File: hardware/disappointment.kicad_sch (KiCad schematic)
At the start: 52 parts, among them J1 Bus_ISA_16bit, J3 Conn_02x10_Odd_Even, J4 Conn_01x02, J5 ATX-24, U1 F85226AF

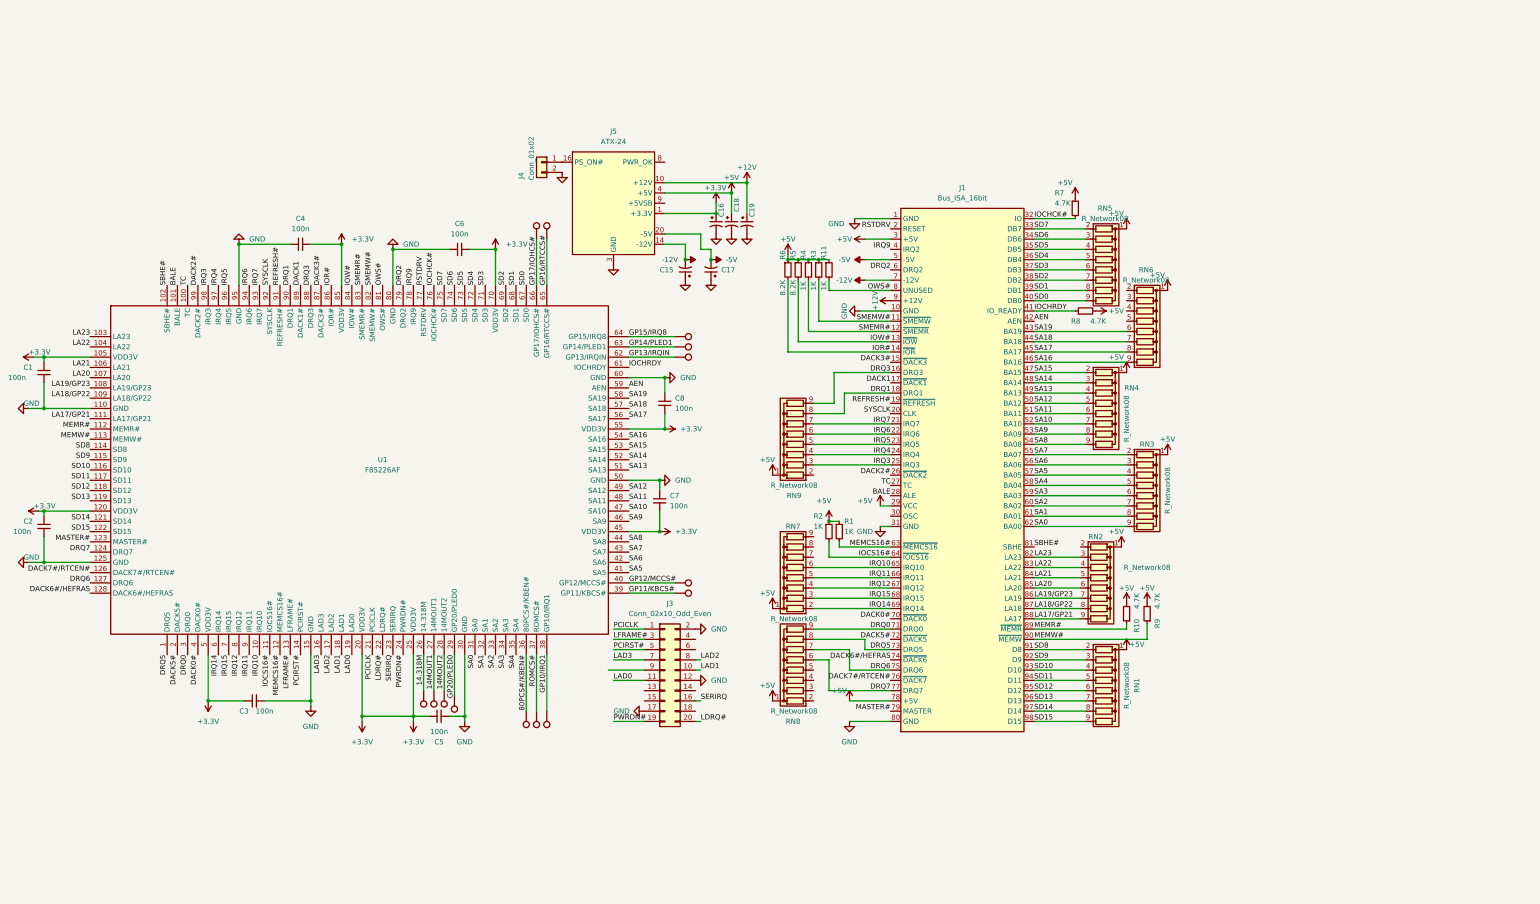
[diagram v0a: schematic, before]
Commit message: started rerouting PCB
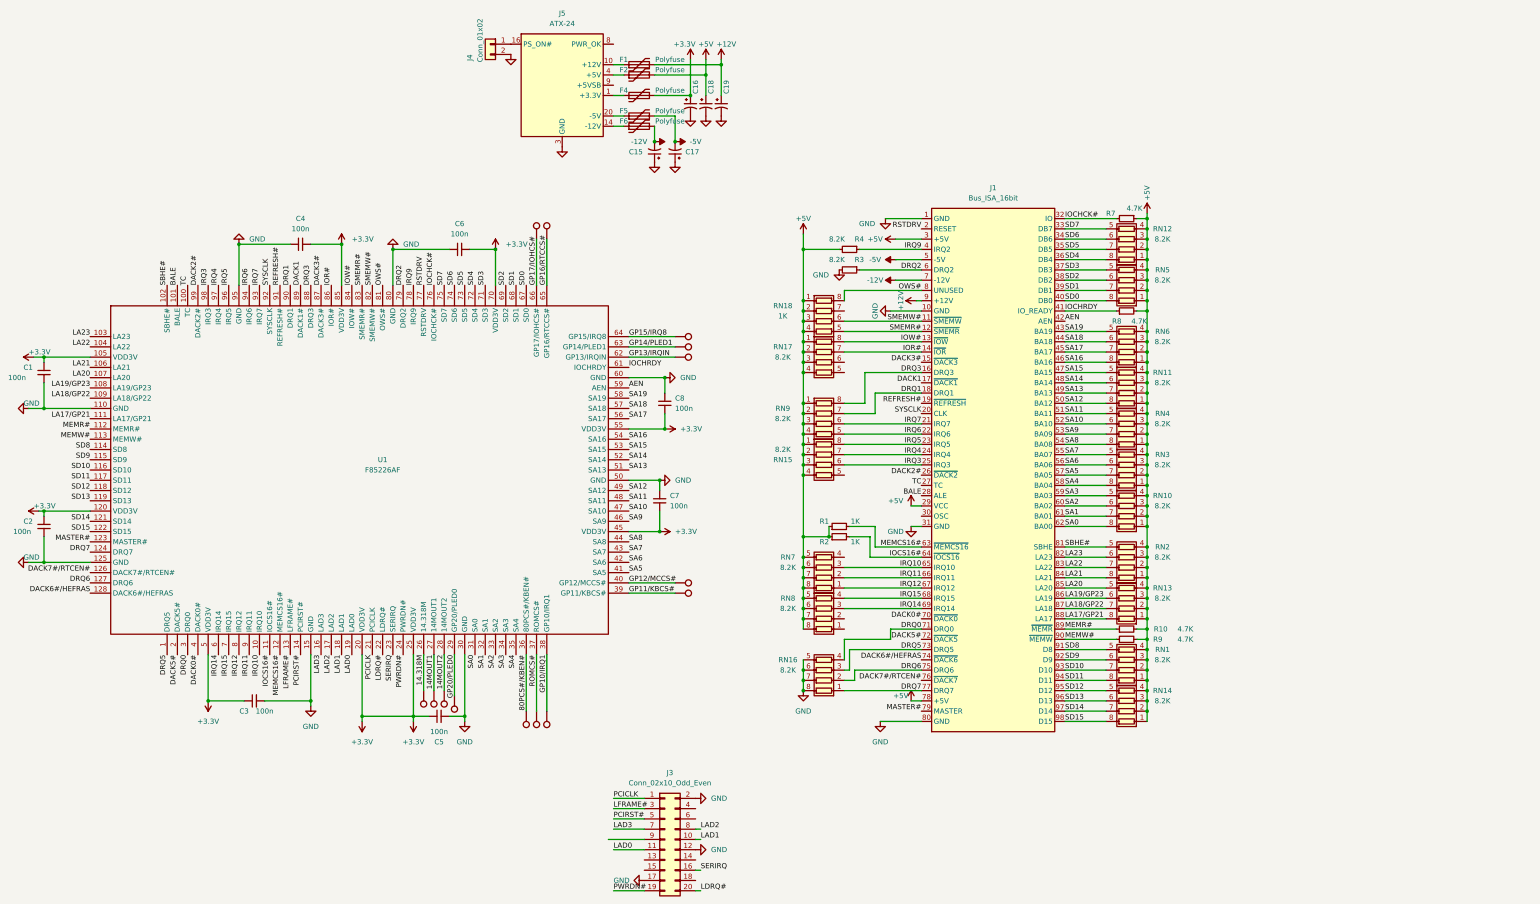
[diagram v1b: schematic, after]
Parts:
- removed R11: 1K, Resistor_SMD:R_1206_3216Metric_Pad1.30x1.75mm_HandSolder, symbol Device:R_Small
- removed R5, R6: 8.2K, Resistor_SMD:R_1206_3216Metric_Pad1.30x1.75mm_HandSolder, symbol Device:R_Small
- removed RN1, RN2, RN3, RN4, RN5, RN6, RN7, RN8, RN9: R_Network08, ps2usb:745C101, symbol Device:R_Network08
- added F1, F2, F4, F5, F6: Polyfuse, symbol Device:Polyfuse
- added RN1, RN10, RN11, RN12, RN13, RN14, RN15, RN16, RN17, RN2, RN3, RN4, RN5, RN6, RN7, RN8, RN9: 8.2K, Resistor_SMD:R_Array_Concave_4x0603, symbol Device:R_Pack04
- added RN18: 1K, Resistor_SMD:R_Array_Concave_4x0603, symbol Device:R_Pack04
- R3, R4: value 1K -> 8.2K
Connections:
- net +12V: now also F1.2; no longer J5.10 (+12V), J5.11 (+12V)
- net +3.3V: now also F4.2; no longer J5.1 (+3.3V), J5.12 (+3.3V), J5.13 (+3.3V), J5.2 (+3.3V)
- net +5V: now also R4.2, F2.2, RN1.1 (R1.1), RN1.2 (R2.1), RN1.3 (R3.1), RN1.4 (R4.1), RN10.1 (R1.1), RN10.2 (R2.1), RN10.3 (R3.1), RN10.4 (R4.1), RN11.1 (R1.1), RN11.2 (R2.1), RN11.3 (R3.1), RN11.4 (R4.1), RN12.1 (R1.1), RN12.2 (R2.1), RN12.3 (R3.1), RN12.4 (R4.1), RN13.1 (R1.1), RN13.2 (R2.1), RN13.3 (R3.1), RN13.4 (R4.1), RN14.1 (R1.1), RN14.2 (R2.1), RN14.3 (R3.1), RN14.4 (R4.1), RN15.1 (R1.1), RN15.2 (R2.1), RN15.3 (R3.1), RN15.4 (R4.1), RN17.1 (R1.1), RN17.2 (R2.1), RN17.3 (R3.1), RN17.4 (R4.1), RN18.1 (R1.1), RN18.2 (R2.1), RN18.3 (R3.1), RN18.4 (R4.1), RN2.1 (R1.1), RN2.2 (R2.1), RN2.3 (R3.1), RN2.4 (R4.1), RN3.1 (R1.1), RN3.2 (R2.1), RN3.3 (R3.1), RN3.4 (R4.1), RN4.1 (R1.1), RN4.2 (R2.1), RN4.3 (R3.1), RN4.4 (R4.1), RN5.1 (R1.1), RN5.2 (R2.1), RN5.3 (R3.1), RN5.4 (R4.1), RN6.1 (R1.1), RN6.2 (R2.1), RN6.3 (R3.1), RN6.4 (R4.1), RN7.5 (R4.2), RN7.6 (R3.2), RN7.7 (R2.2), RN7.8 (R1.2), RN8.5 (R4.2), RN8.6 (R3.2), RN8.7 (R2.2), RN8.8 (R1.2), RN9.1 (R1.1), RN9.2 (R2.1), RN9.3 (R3.1), RN9.4 (R4.1); no longer J5.21 (+5V), J5.22 (+5V), J5.23 (+5V), J5.4 (+5V), J5.6 (+5V), R3.1, R4.1
- net -12V: now also F6.2; no longer J5.14 (-12V)
- net -5V: now also F5.2; no longer J5.20 (NC)
- net DRQ0: now also RN16.4 (R4.1)
- net DRQ1: now also RN9.7 (R2.2)
- net DRQ2: now also R3.1
- net DRQ3: now also RN9.8 (R1.2)
- net DRQ5: now also RN16.3 (R3.1)
- net DRQ6: now also RN16.2 (R2.1)
- net DRQ7: now also RN16.1 (R1.1)
- net GND: now also R3.2, RN16.5 (R4.2), RN16.6 (R3.2), RN16.7 (R2.2), RN16.8 (R1.2)
- net IOR#: now also RN17.7 (R2.2)
- net IOW#: now also RN17.8 (R1.2)
- net IRQ10: now also RN7.3 (R3.1)
- net IRQ11: now also RN7.2 (R2.1)
- net IRQ12: now also RN7.1 (R1.1)
- net IRQ14: now also RN8.3 (R3.1)
- net IRQ15: now also RN8.4 (R4.1)
- net IRQ3: now also RN15.6 (R3.2)
- net IRQ4: now also RN15.7 (R2.2)
- net IRQ5: now also RN15.8 (R1.2)
- net IRQ6: now also RN9.5 (R4.2)
- net IRQ7: now also RN9.6 (R3.2)
- net IRQ9: now also R4.1
- net LA17/GP21: now also RN13.8 (R1.2)
- net LA18/GP22: now also RN13.7 (R2.2)
- net LA19/GP23: now also RN13.6 (R3.2)
- net LA20: now also RN13.5 (R4.2)
- net LA21: now also RN2.8 (R1.2)
- net LA22: now also RN2.7 (R2.2)
- net LA23: now also RN2.6 (R3.2)
- net OWS#: now also RN18.8 (R1.2)
- net SA0: now also RN10.8 (R1.2)
- net SA1: now also RN10.7 (R2.2)
- net SA10: now also RN4.6 (R3.2)
- net SA11: now also RN4.5 (R4.2)
- net SA12: now also RN11.8 (R1.2)
- net SA13: now also RN11.7 (R2.2)
- net SA14: now also RN11.6 (R3.2)
- net SA15: now also RN11.5 (R4.2)
- net SA16: now also RN6.8 (R1.2)
- net SA17: now also RN6.7 (R2.2)
- net SA18: now also RN6.6 (R3.2)
- net SA19: now also RN6.5 (R4.2)
- net SA2: now also RN10.6 (R3.2)
- net SA3: now also RN10.5 (R4.2)
- net SA4: now also RN3.8 (R1.2)
- net SA5: now also RN3.7 (R2.2)
- net SA6: now also RN3.6 (R3.2)
- net SA7: now also RN3.5 (R4.2)
- net SA8: now also RN4.8 (R1.2)
- net SA9: now also RN4.7 (R2.2)
- net SBHE#: now also RN2.5 (R4.2)
- net SD0: now also RN5.8 (R1.2)
- net SD1: now also RN5.7 (R2.2)
- net SD10: now also RN1.7 (R2.2)
- net SD11: now also RN1.8 (R1.2)
- net SD12: now also RN14.5 (R4.2)
- net SD13: now also RN14.6 (R3.2)
- net SD14: now also RN14.7 (R2.2)
- net SD15: now also RN14.8 (R1.2)
- net SD2: now also RN5.6 (R3.2)
- net SD3: now also RN5.5 (R4.2)
- net SD4: now also RN12.8 (R1.2)
- net SD5: now also RN12.7 (R2.2)
- net SD6: now also RN12.6 (R3.2)
- net SD7: now also RN12.5 (R4.2)
- net SD8: now also RN1.5 (R4.2)
- net SD9: now also RN1.6 (R3.2)
- net SMEMR#: now also RN18.5 (R4.2); no longer R4.2
- net SMEMW#: now also RN18.6 (R3.2); no longer R3.2
- net at J5.20 (NC): now also F5.1
- new net: F6.1, J5.14 (-12V)
- new net: F2.1, J5.21 (+5V), J5.22 (+5V), J5.23 (+5V), J5.4 (+5V), J5.6 (+5V)
- new net: F4.1, J5.1 (+3.3V), J5.12 (+3.3V), J5.13 (+3.3V), J5.2 (+3.3V)
- new net: F1.1, J5.10 (+12V), J5.11 (+12V)
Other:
- moved on the sheet: C15, C16, C17, C18, C19, J1, J3, J4, J5, R1, R10, R2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

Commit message: getting there
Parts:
- F1, F2, F4, F5, F6: footprint (none) -> Fuse:Fuse_1206_3216Metric
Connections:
- net DRQ0: now also RN16.1 (R1.1); no longer RN16.4 (R4.1)
- net DRQ5: now also RN16.2 (R2.1); no longer RN16.3 (R3.1)
- net DRQ6: now also RN16.3 (R3.1); no longer RN16.2 (R2.1)
- net DRQ7: now also RN16.4 (R4.1); no longer RN16.1 (R1.1)
- net IRQ10: now also RN7.2 (R2.1); no longer RN7.3 (R3.1)
- net IRQ11: now also RN7.3 (R3.1); no longer RN7.2 (R2.1)
- net IRQ12: now also RN7.4 (R4.1); no longer RN7.1 (R1.1)
- net IRQ14: now also RN8.2 (R2.1); no longer RN8.3 (R3.1)
- net IRQ15: now also RN8.1 (R1.1); no longer RN8.4 (R4.1)
- net at J5.20 (NC): now also F5.1

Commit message: getting there more
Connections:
- net OWS#: now also RN18.5 (R4.2); no longer RN18.8 (R1.2)
- net SMEMR#: now also RN18.8 (R1.2); no longer RN18.5 (R4.2)
- net SMEMW#: now also RN18.7 (R2.2); no longer RN18.6 (R3.2)
- net at J5.20 (NC): now also F5.1
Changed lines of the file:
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@@
   (junction (at 397.51 251.46) (diameter 0) (color 0 0 0 0)
   )
-  (junction (at 312.42 160.02) (diameter 0) (color 0 0 0 0)
-  )
   (junction (at 397.51 185.42) (diameter 0) (color 0 0 0 0)
   )
@@
   (junction (at 318.77 218.44) (diameter 0) (color 0 0 0 0)
   )
-  (junction (at 312.42 165.1) (diameter 0) (color 0 0 0 0)
-  )
   (junction (at 278.13 191.77) (diameter 0) (color 0 0 0 0)
   )
@@
   (junction (at 215.9 262.89) (diameter 0) (color 0 0 0 0)
   )
-  (junction (at 312.42 167.64) (diameter 0) (color 0 0 0 0)
-  )
   (junction (at 397.51 220.98) (diameter 0) (color 0 0 0 0)
   )
   (junction (at 280.67 120.65) (diameter 0) (color 0 0 0 0)
   )
+  (junction (at 312.42 165.1) (diameter 0) (color 0 0 0 0)
+  )
   (junction (at 397.51 193.04) (diameter 0) (color 0 0 0 0)
   )
@@
   (junction (at 397.51 175.26) (diameter 0) (color 0 0 0 0)
   )
-  (junction (at 312.42 162.56) (diameter 0) (color 0 0 0 0)
-  )
   (junction (at 397.51 203.2) (diameter 0) (color 0 0 0 0)
   )
@@
   (junction (at 198.12 146.05) (diameter 0) (color 0 0 0 0)
   )
+  (junction (at 312.42 167.64) (diameter 0) (color 0 0 0 0)
+  )
   (junction (at 312.42 172.72) (diameter 0) (color 0 0 0 0)
   )
@@
   (junction (at 284.48 109.22) (diameter 0) (color 0 0 0 0)
   )
+  (junction (at 312.42 162.56) (diameter 0) (color 0 0 0 0)
+  )
   (junction (at 312.42 236.22) (diameter 0) (color 0 0 0 0)
   )
@@
   (junction (at 312.42 195.58) (diameter 0) (color 0 0 0 0)
   )
+  (junction (at 312.42 160.02) (diameter 0) (color 0 0 0 0)
+  )
   (junction (at 397.51 149.86) (diameter 0) (color 0 0 0 0)
   )
@@
     (stroke (width 0) (type default))
   )
-  (wire (pts (xy 312.42 160.02) (xy 312.42 162.56))
+  (wire (pts (xy 312.42 147.32) (xy 312.42 160.02))
     (stroke (width 0) (type default))
   )
@@
     (stroke (width 0) (type default))
   )
-  (wire (pts (xy 312.42 147.32) (xy 312.42 160.02))
-    (stroke (width 0) (type default))
-  )
   (wire (pts (xy 312.42 170.18) (xy 312.42 172.72))
     (stroke (width 0) (type default))
@@
     (stroke (width 0) (type default))
   )
+  (wire (pts (xy 312.42 162.56) (xy 312.42 165.1))
+    (stroke (width 0) (type default))
+  )
   (wire (pts (xy 341.63 177.8) (xy 327.66 177.8))
     (stroke (width 0) (type default))
@@
     (stroke (width 0) (type default))
   )
+  (wire (pts (xy 312.42 167.64) (xy 312.42 170.18))
+    (stroke (width 0) (type default))
+  )
   (wire (pts (xy 397.51 233.68) (xy 397.51 236.22))
     (stroke (width 0) (type default))
@@
     (stroke (width 0) (type default))
   )
-  (wire (pts (xy 312.42 167.64) (xy 312.42 170.18))
-    (stroke (width 0) (type default))
-  )
   (wire (pts (xy 387.35 149.86) (xy 377.19 149.86))
     (stroke (width 0) (type default))
@@
     (stroke (width 0) (type default))
   )
+  (wire (pts (xy 312.42 160.02) (xy 312.42 162.56))
+    (stroke (width 0) (type default))
+  )
   (wire (pts (xy 284.48 100.33) (xy 284.48 109.22))
     (stroke (width 0) (type default))
@@
     (stroke (width 0) (type default))
   )
-  (wire (pts (xy 312.42 162.56) (xy 312.42 165.1))
-    (stroke (width 0) (type default))
-  )
   (wire (pts (xy 312.42 195.58) (xy 312.42 198.12))
     (stroke (width 0) (type default))
@@
     )
   )
+  (symbol (lib_id "Device:R_Pack04") (at 317.5 162.56 270) (mirror x) (unit 1)
+    (in_bom yes) (on_board yes) (dnp no)
+    (property "Reference" "RN18" (at 307.34 166.37 90)
+      (effects (font (size 1.27 1.27)))
+    )
+    (property "Value" "1K" (at 307.34 163.83 90)
+      (effects (font (size 1.27 1.27)))
+    )
+    (property "Footprint" "Resistor_SMD:R_Array_Concave_4x0603" (at 317.5 155.575 90)
+      (effects (font (size 1.27 1.27)) hide)
+    )
+    (property "Datasheet" "~" (at 317.5 162.56 0)
+      (effects (font (size 1.27 1.27)) hide)
+    )
+    (pin "1")
+    (pin "2")
+    (pin "3")
+    (pin "4")
+    (pin "5")
+    (pin "6")
+    (pin "7")
+    (pin "8")
+    (instances
+      (project "disappointment"
+        (path "/a1292a79-9ba8-4ff9-9f33-166186bea326"
+          (reference "RN18") (unit 1)
+        )
+      )
+    )
+  )
   (symbol (lib_id "Device:R_Pack04") (at 392.43 248.92 90) (unit 1)
     (in_bom yes) (on_board yes) (dnp no)
@@
         )
       )
-    )
-  )
-  (symbol (lib_id "Device:R_Pack04") (at 317.5 165.1 270) (unit 1)
-    (in_bom yes) (on_board yes) (dnp no)
-    (property "Reference" "RN18" (at 307.34 161.29 90)
-      (effects (font (size 1.27 1.27)))
-    )
-    (property "Value" "1K" (at 307.34 163.83 90)
-      (effects (font (size 1.27 1.27)))
-    )
-    (property "Footprint" "Resistor_SMD:R_Array_Concave_4x0603" (at 317.5 172.085 90)
-      (effects (font (size 1.27 1.27)) hide)
-    )
-    (property "Datasheet" "~" (at 317.5 165.1 0)
-      (effects (font (size 1.27 1.27)) hide)
-    )
-    (pin "1")
-    (pin "2")
-    (pin "3")
-    (pin "4")
-    (pin "5")
-    (pin "6")
-    (pin "7")
-    (pin "8")
-    (instances
-      (project "disappointment"
-        (path "/a1292a79-9ba8-4ff9-9f33-166186bea326"
-          (reference "RN18") (unit 1)
-        )
-      )

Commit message: about done
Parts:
- removed J4: Conn_01x02, Connector_PinHeader_2.54mm:PinHeader_1x02_P2.54mm_Vertical, symbol Connector_Generic:Conn_01x02
- removed TP1, TP10, TP11, TP12, TP13, TP14, TP2, TP3, TP4, TP5, TP6, TP7, TP8, TP9: TestPoint, TestPoint:TestPoint_THTPad_2.0x2.0mm_Drill1.0mm, symbol Connector:TestPoint
- added R5: 10K, Resistor_SMD:R_1206_3216Metric_Pad1.30x1.75mm_HandSolder, symbol Device:R_Small
- added R6: DNP, Resistor_SMD:R_1206_3216Metric_Pad1.30x1.75mm_HandSolder, symbol Device:R_Small
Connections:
- net +5V: now also RN18.5 (R4.2), RN18.6 (R3.2), RN18.7 (R2.2), RN18.8 (R1.2); no longer RN18.1 (R1.1), RN18.2 (R2.1), RN18.3 (R3.1), RN18.4 (R4.1)
- net DACK6#/HEFRAS: now also R6.2
- net GND: now also R5.1, R6.1
- net OWS#: now also RN18.4 (R4.1); no longer RN18.5 (R4.2)
- net ROMCS#: now also R5.2
- net SMEMR#: now also RN18.1 (R1.1); no longer RN18.8 (R1.2)
- net SMEMW#: now also RN18.2 (R2.1); no longer RN18.7 (R2.2)
- net at J5.20 (NC): now also F5.1
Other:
- moved on the sheet: C15, C16, C17, C18, C19, F1, F2, F4, F5, F6, J1, J3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

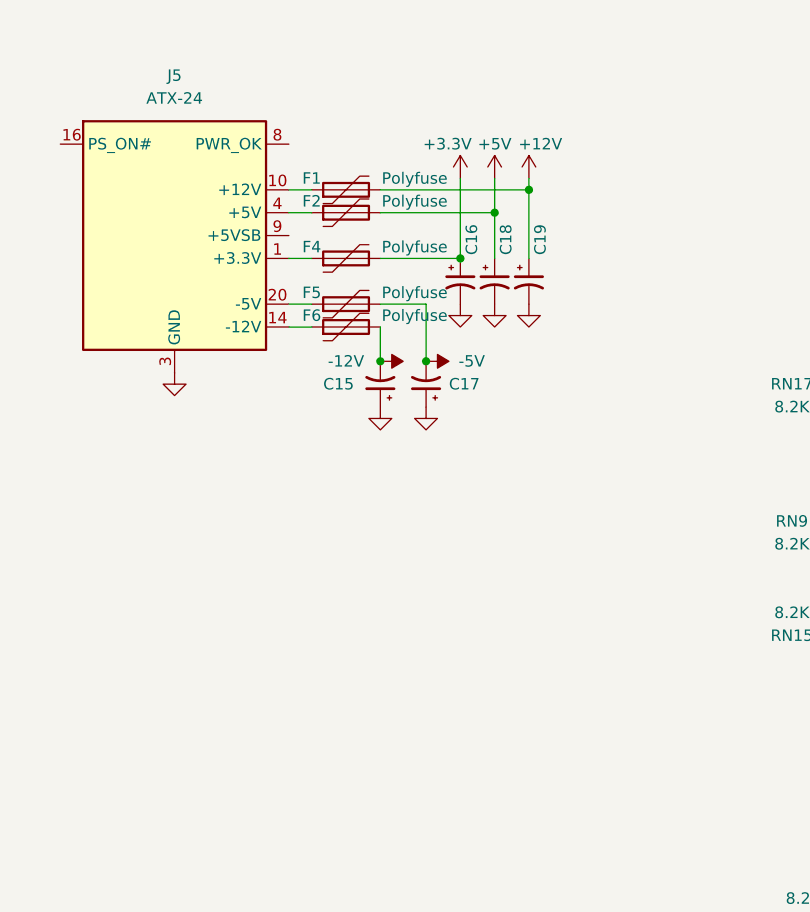
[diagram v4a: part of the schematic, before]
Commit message: LEDs, -5v regulator
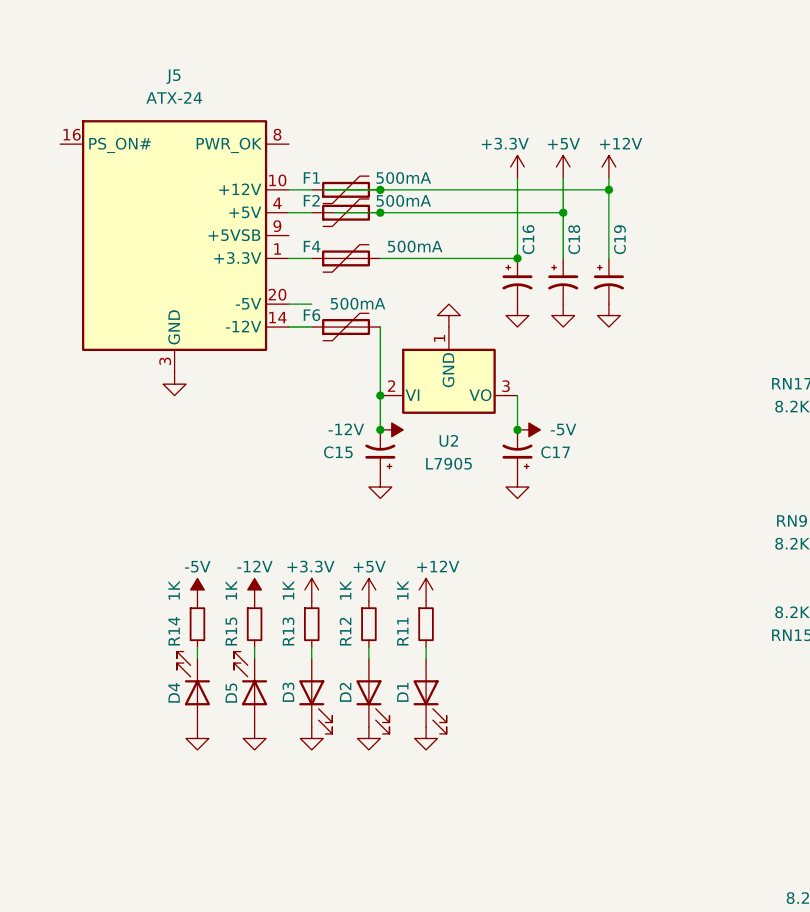
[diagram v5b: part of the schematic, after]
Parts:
- removed F5: Polyfuse, Fuse:Fuse_1206_3216Metric, symbol Device:Polyfuse
- added D1, D2, D3, D4, D5: LED, LED_SMD:LED_1206_3216Metric, symbol Device:LED
- added R11, R12, R13, R14, R15: 1K, Resistor_SMD:R_1206_3216Metric_Pad1.30x1.75mm_HandSolder, symbol Device:R_Small
- added U2: L7905, Package_TO_SOT_THT:TO-220-3_Vertical, symbol Regulator_Linear:L7905
- F1, F2, F4, F6: value Polyfuse -> 500mA
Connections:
- net +12V: now also R11.1
- net +3.3V: now also R13.1
- net +5V: now also R12.1
- net -12V: now also R15.1, U2.2 (VI)
- net -5V: now also R14.1, U2.3 (VO)
- net GND: now also D1.1 (K), D2.1 (K), D3.1 (K), D4.2 (A), D5.2 (A), U2.1 (GND)
- new net: D3.2 (A), R13.2
- new net: D1.2 (A), R11.2
- new net: D4.1 (K), R14.2
- new net: D2.2 (A), R12.2
- new net: D5.1 (K), R15.2
- now unconnected: J5.20 (NC)
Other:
- moved on the sheet: C15, C16, C17, C18, C19
